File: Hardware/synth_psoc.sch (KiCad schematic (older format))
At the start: 0 parts

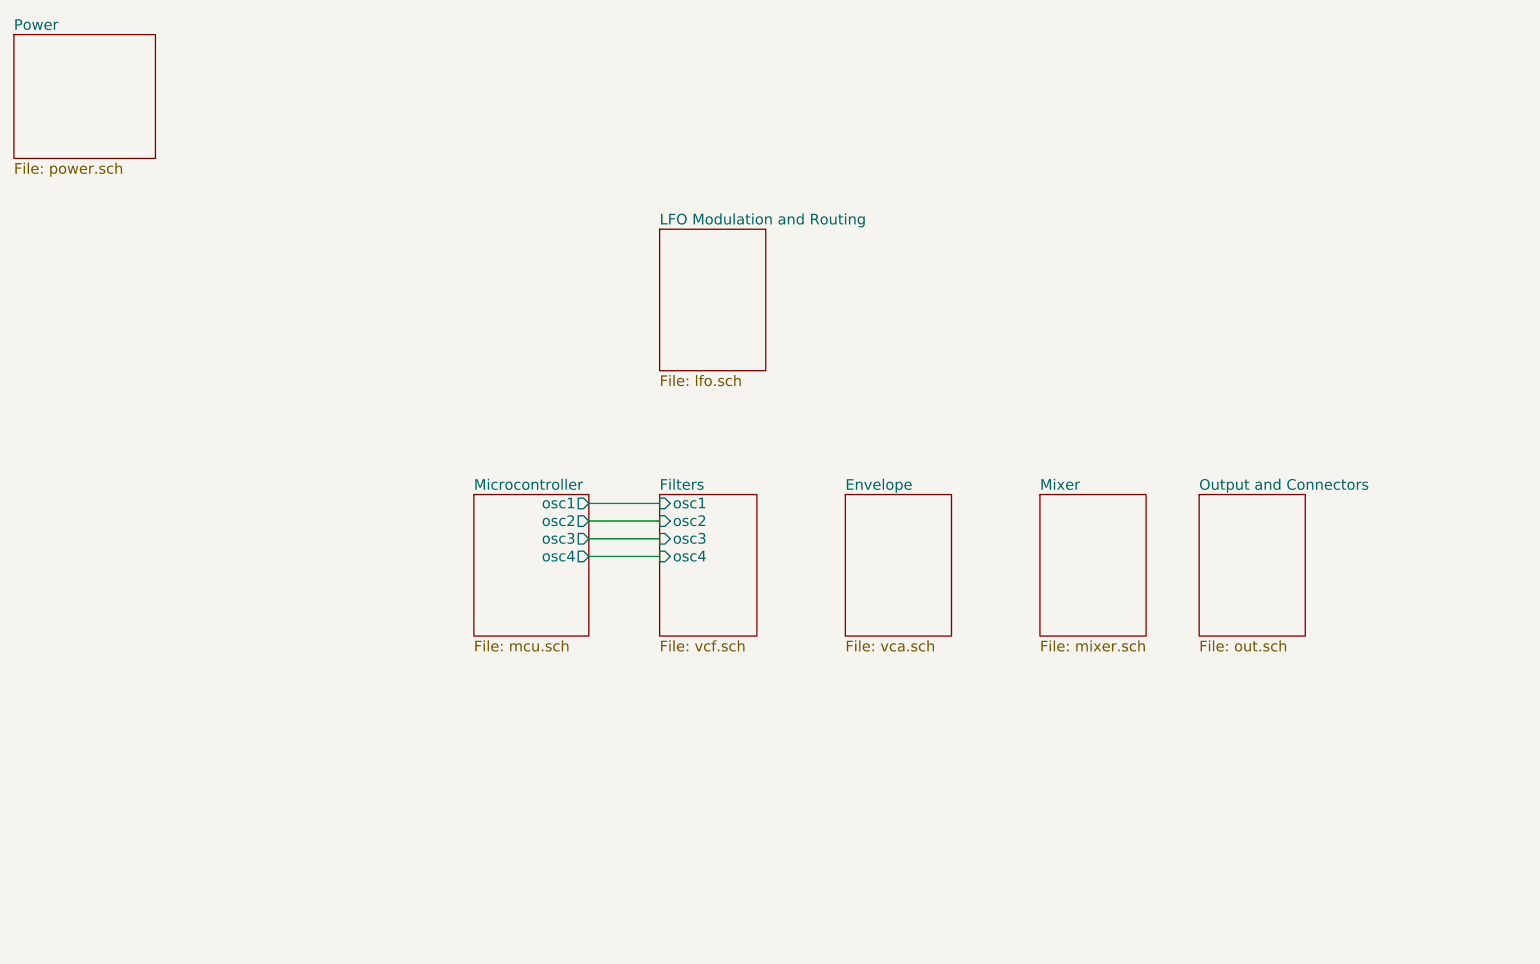
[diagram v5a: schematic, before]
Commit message: complete wiring of top level schematic hierarchical pages
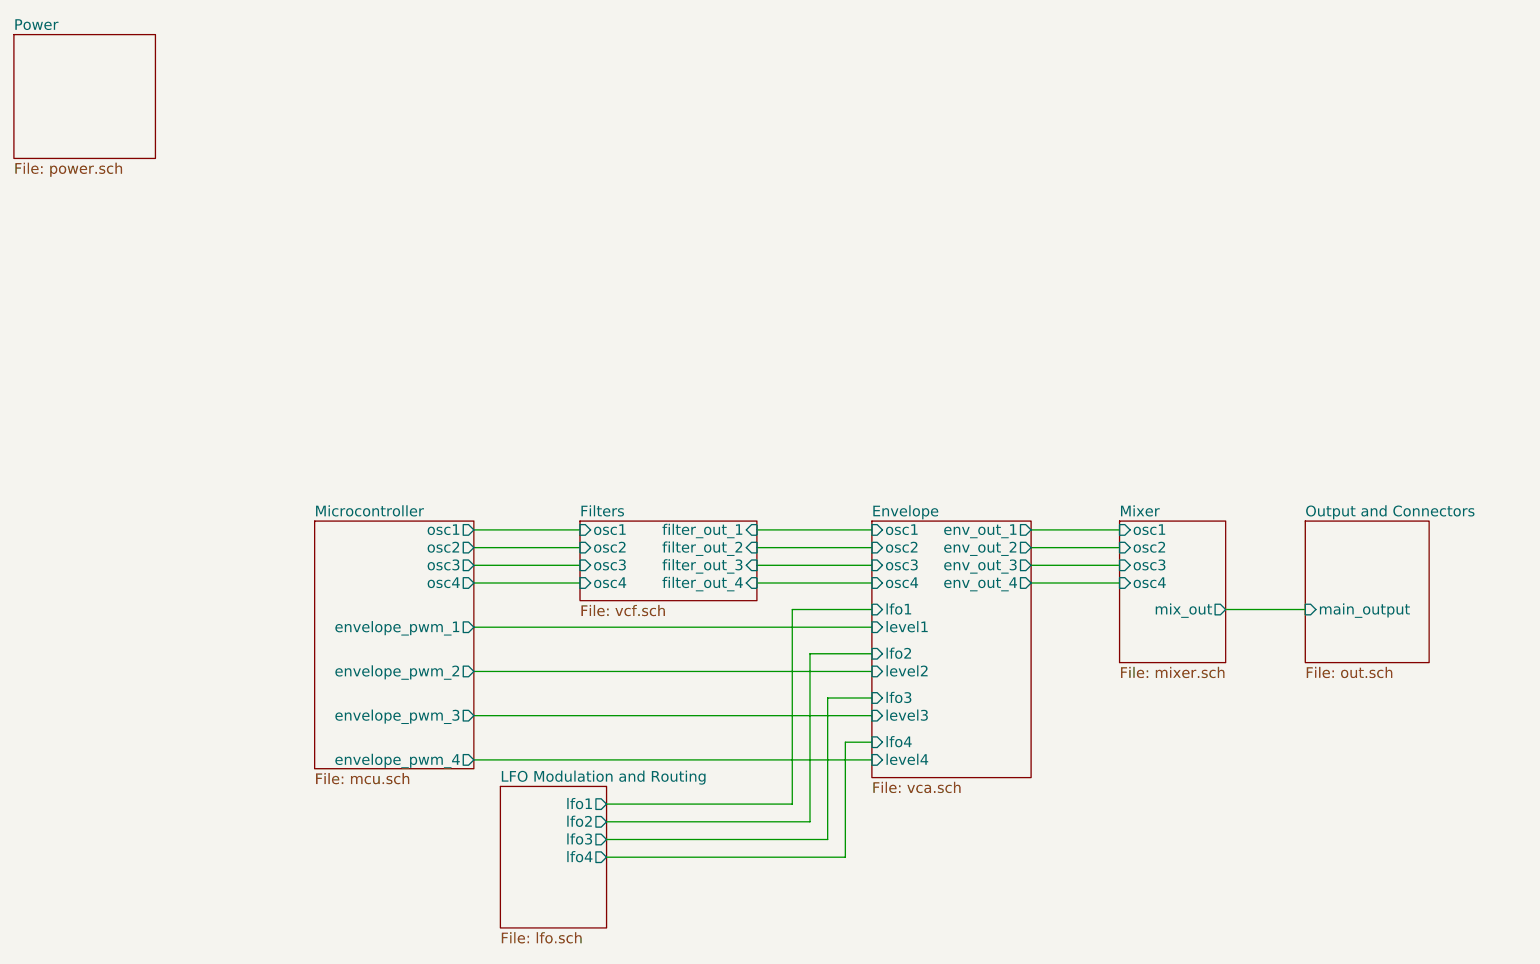
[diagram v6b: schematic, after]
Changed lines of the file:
@@
 $EndDescr
 $Sheet
-S 3250 3250 650  800
-U 5C3546FC
-F0 "Microcontroller" 60
-F1 "mcu.sch" 60
-F2 "osc1" O R 3900 3300 60
-F3 "osc2" O R 3900 3400 60
-F4 "osc3" O R 3900 3500 60
-F5 "osc4" O R 3900 3600 60
-$EndSheet
-$Sheet
-S 4300 3250 550  800
+S 3850 3400 1000 450
 U 5C355489
 F0 "Filters" 60
 F1 "vcf.sch" 60
-F2 "osc1" I L 4300 3300 60
-F3 "osc2" I L 4300 3400 60
-F4 "osc3" I L 4300 3500 60
-F5 "osc4" I L 4300 3600 60
+F2 "osc1" I L 3850 3450 60
+F3 "osc2" I L 3850 3550 60
+F4 "osc3" I L 3850 3650 60
+F5 "osc4" I L 3850 3750 60
+F6 "filter_out_1" I R 4850 3450 60
+F7 "filter_out_2" I R 4850 3550 60
+F8 "filter_out_3" I R 4850 3650 60
+F9 "filter_out_4" I R 4850 3750 60
 $EndSheet
-Wire Wire Line
-	3900 3300 4300 3300
-Wire Wire Line
-	3900 3400 4300 3400
-Wire Wire Line
-	3900 3500 4300 3500
-Wire Wire Line
-	3900 3600 4300 3600
 $Sheet
 S 650  650  800  700
@@
 $EndSheet
 $Sheet
-S 5350 3250 600  800
+S 5500 3400 900  1450
 U 5C356D9E
 F0 "Envelope" 60
 F1 "vca.sch" 60
+F2 "osc1" I L 5500 3450 60
+F3 "osc2" I L 5500 3550 60
+F4 "osc3" I L 5500 3650 60
+F5 "osc4" I L 5500 3750 60
+F6 "lfo1" I L 5500 3900 60
+F7 "level1" I L 5500 4000 60
+F8 "env_out_1" O R 6400 3450 60
+F9 "lfo2" I L 5500 4150 60
+F10 "level2" I L 5500 4250 60
+F11 "env_out_2" O R 6400 3550 60
+F12 "lfo3" I L 5500 4400 60
+F13 "level3" I L 5500 4500 60
+F14 "env_out_3" O R 6400 3650 60
+F15 "lfo4" I L 5500 4650 60
+F16 "level4" I L 5500 4750 60
+F17 "env_out_4" O R 6400 3750 60
 $EndSheet
 $Sheet
-S 6450 3250 600  800
+S 6900 3400 600  800
 U 5C357081
 F0 "Mixer" 60
 F1 "mixer.sch" 60
+F2 "osc1" I L 6900 3450 60
+F3 "osc2" I L 6900 3550 60
+F4 "osc3" I L 6900 3650 60
+F5 "osc4" I L 6900 3750 60
+F6 "mix_out" O R 7500 3900 60
 $EndSheet
 $Sheet
-S 4300 1750 600  800
+S 3400 4900 600  800
 U 5C35738C
 F0 "LFO Modulation and Routing" 60
 F1 "lfo.sch" 60
+F2 "lfo1" O R 4000 5000 60
+F3 "lfo2" O R 4000 5100 60
+F4 "lfo3" O R 4000 5200 60
+F5 "lfo4" O R 4000 5300 60
 $EndSheet
 $Sheet
-S 7350 3250 600  800
+S 7950 3400 700  800
 U 5C357E40
 F0 "Output and Connectors" 60
 F1 "out.sch" 60
+F2 "main_output" I L 7950 3900 60
 $EndSheet
+Wire Wire Line
+	3250 3450 3850 3450
+Wire Wire Line
+	3250 3550 3850 3550
+Wire Wire Line
+	3250 3650 3850 3650
+Wire Wire Line
+	3250 3750 3850 3750
+Wire Wire Line
+	4850 3450 5500 3450
+Wire Wire Line
+	4850 3550 5500 3550
+Wire Wire Line
+	4850 3650 5500 3650
+Wire Wire Line
+	4850 3750 5500 3750
+Wire Wire Line
+	6400 3450 6900 3450
+Wire Wire Line
+	6400 3550 6900 3550
+Wire Wire Line
+	6400 3650 6900 3650
+Wire Wire Line
+	6400 3750 6900 3750
+Wire Wire Line
+	4000 5000 5050 5000
+Wire Wire Line
+	5050 5000 5050 3900
+Wire Wire Line
+	5050 3900 5500 3900
+Wire Wire Line
+	5500 4150 5150 4150
+Wire Wire Line
+	5150 4150 5150 5100
+Wire Wire Line
+	5150 5100 4000 5100
+Wire Wire Line
+	5500 4400 5250 4400
+Wire Wire Line
+	5250 4400 5250 5200
+Wire Wire Line
+	5250 5200 4000 5200
+Wire Wire Line
+	5500 4650 5350 4650
+Wire Wire Line
+	5350 4650 5350 5300
+Wire Wire Line
+	5350 5300 4000 5300
+$Sheet
+S 2350 3400 900  1400
+U 5C3546FC
+F0 "Microcontroller" 60
+F1 "mcu.sch" 60
+F2 "osc1" O R 3250 3450 60
+F3 "osc2" O R 3250 3550 60
+F4 "osc3" O R 3250 3650 60
+F5 "osc4" O R 3250 3750 60
+F6 "envelope_pwm_1" O R 3250 4000 60
+F7 "envelope_pwm_2" O R 3250 4250 60
+F8 "envelope_pwm_3" O R 3250 4500 60
+F9 "envelope_pwm_4" O R 3250 4750 60
+$EndSheet
+Wire Wire Line
+	3250 4000 5500 4000
+Wire Wire Line
+	5500 4250 3250 4250
+Wire Wire Line
+	3250 4500 5500 4500
+Wire Wire Line
+	5500 4750 3250 4750
+Wire Wire Line
+	7950 3900 7500 3900
 $EndSCHEMATC

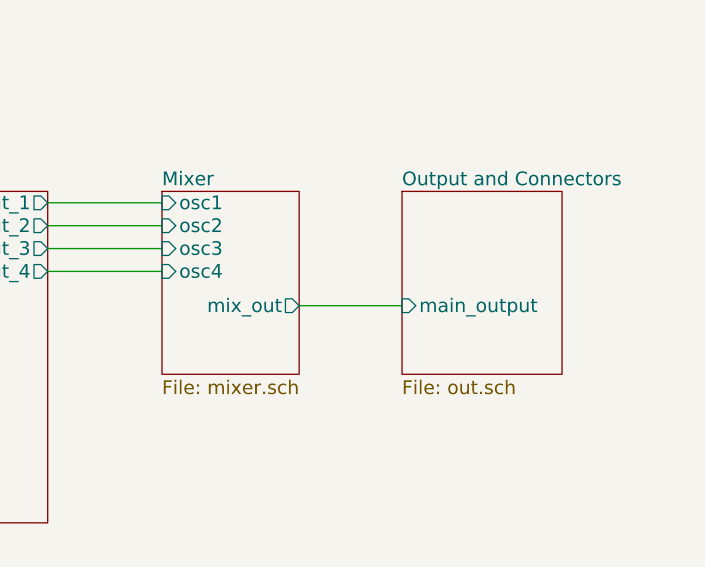
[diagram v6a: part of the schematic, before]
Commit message: add VREF to all single supply op amps
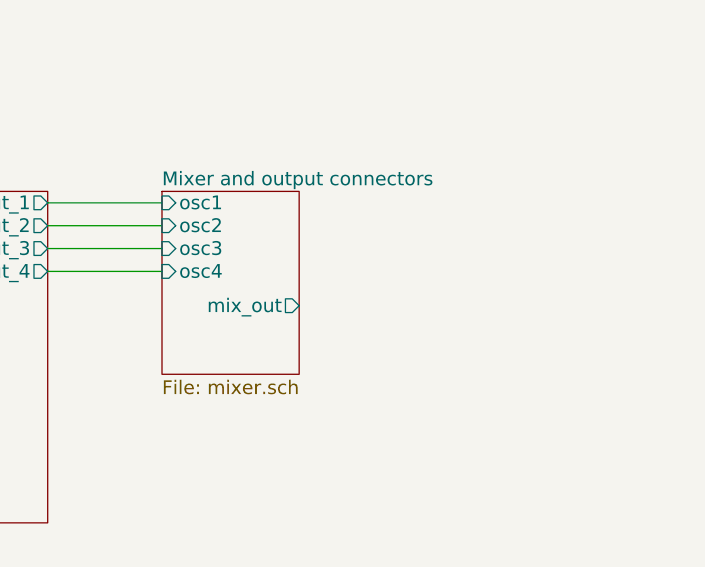
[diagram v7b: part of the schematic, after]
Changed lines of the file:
@@
 $Descr A4 11693 8268
 encoding utf-8
-Sheet 1 8
+Sheet 1 7
 Title ""
 Date ""
@@
 S 6900 3400 600  800
 U 5C357081
-F0 "Mixer" 60
+F0 "Mixer and output connectors" 60
 F1 "mixer.sch" 60
 F2 "osc1" I L 6900 3450 60
@@
 F4 "lfo3" O R 4000 5200 60
 F5 "lfo4" O R 4000 5300 60
-$EndSheet
-$Sheet
-S 7950 3400 700  800
-U 5C357E40
-F0 "Output and Connectors" 60
-F1 "out.sch" 60
-F2 "main_output" I L 7950 3900 60
 $EndSheet
 Wire Wire Line
@@
 Wire Wire Line
 	5500 4750 3250 4750
-Wire Wire Line
-	7950 3900 7500 3900
 $EndSCHEMATC
